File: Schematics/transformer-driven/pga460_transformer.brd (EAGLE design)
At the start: 20 parts, among them IC1 PGA460TPWQ1, T1 B78416A2232A003

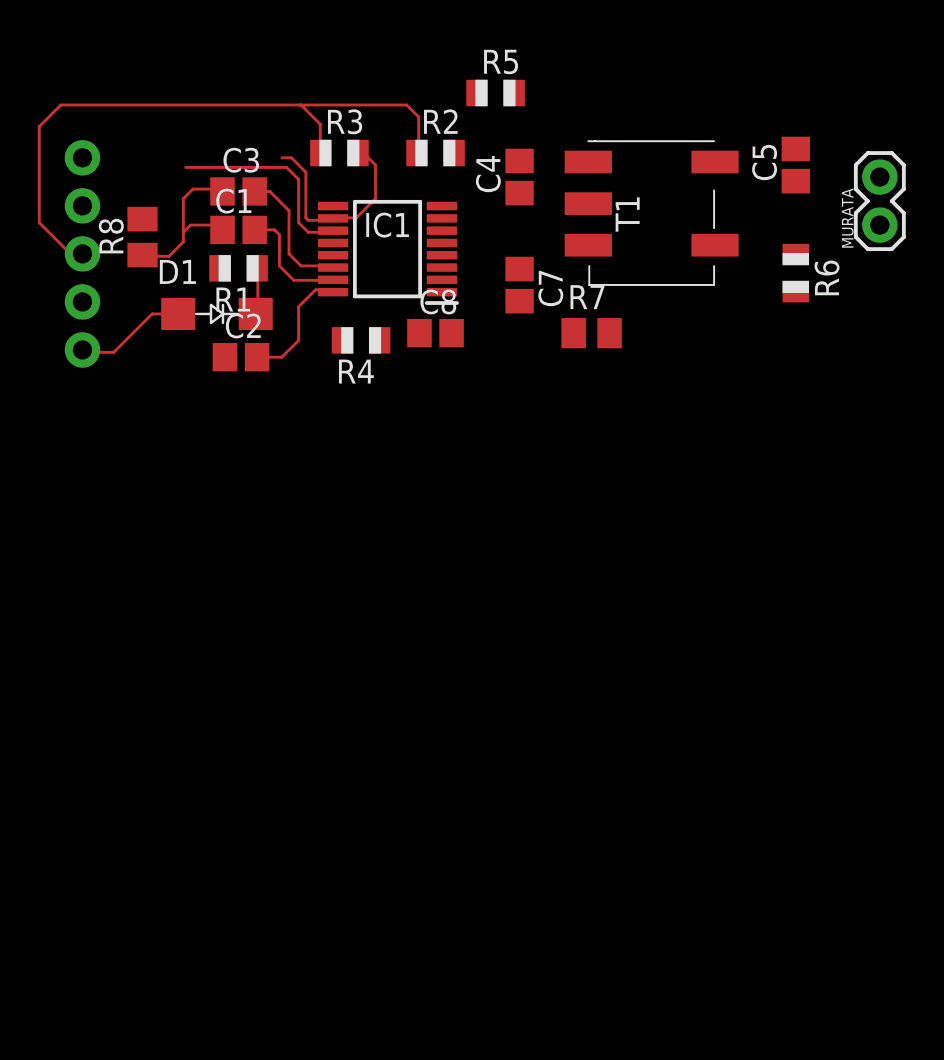
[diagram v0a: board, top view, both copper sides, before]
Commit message: update report. add in mega shield template.
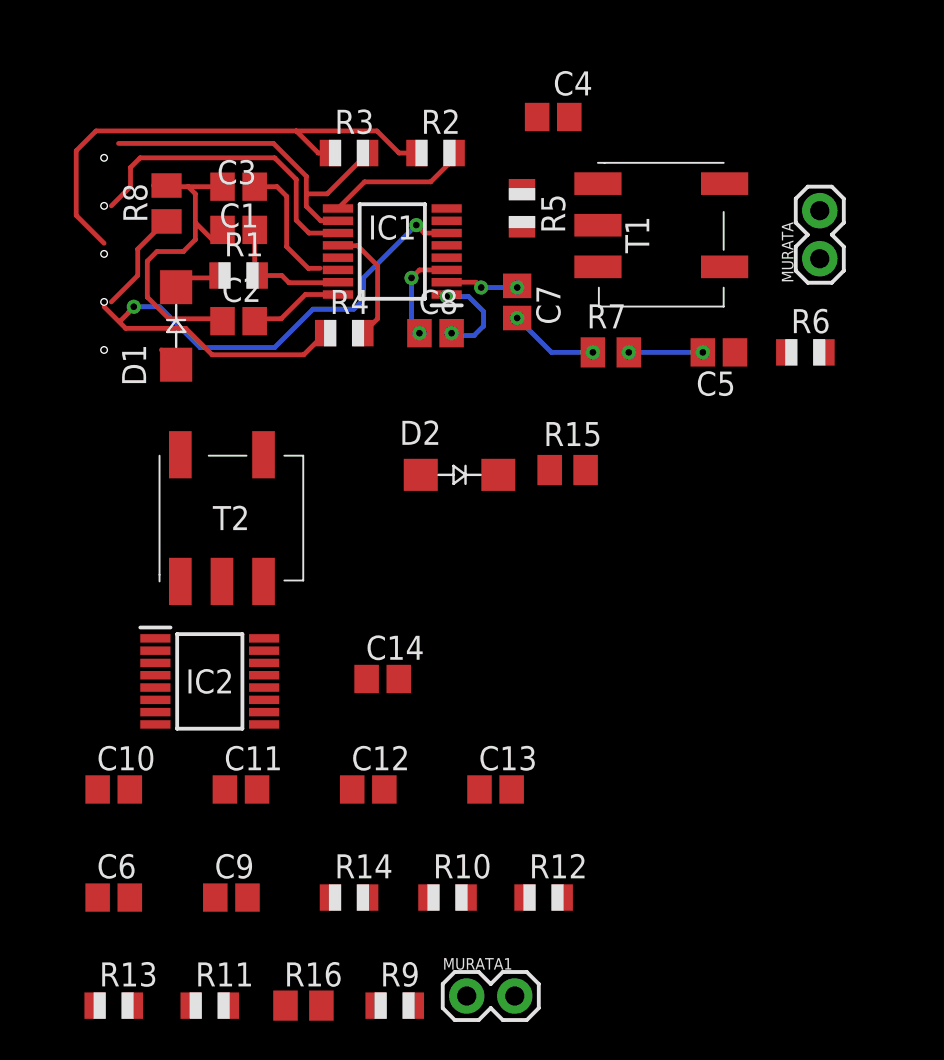
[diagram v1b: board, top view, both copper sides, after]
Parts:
- removed J1: (no value), SparkFun-Connectors:1X05
- added C10: 100uF, adafruit:C0805
- added C11: 680pF, adafruit:C0805
- added C12: 0.1 uF, adafruit:C0805
- added C13: 390pF, adafruit:C0805
- added C14: 0.033uF, adafruit:C0805
- added C6, C9: 0.1uF, adafruit:C0805
- added D2: 1N4007, casovac:SMA
- added IC2: PGA460TPWQ1, PGA460TPWQ1:SOP65P640X120-16N
- added MURATA1: ma59mf14-7n, SparkFun-Connectors:1X02
- added R10, R11, R12: 10k, adafruit:R0805
- added R13: 100, adafruit:R0805
- added R14: 2.7k, adafruit:R0805
- added R15: 3K, rcl:M0805
- added R16: 0, adafruit:M0805
- added R9: 10, adafruit:R0805
- added T2: B78416A2232A003, SamacSys_Parts:B78416A2232A003
- moved C5 10.7 mm to (14.2, -34.7), turned to 180 degrees
- moved R5 6.25 mm to (3.81, -27.1), turned to 270 degrees
- moved R6 4.22 mm to (18.8, -34.7), turned to 0 degrees
- moved MURATA 3.64 mm to (19.6, -29.7)
- moved C4 3.64 mm to (5.46, -22.2), turned to 0 degrees
- moved D1 2.25 mm to (-14.5, -33.3), turned to 90 degrees
- moved R8 2.18 mm to (-15.0, -26.8)
- moved C2 1.91 mm to (-11.2, -33.0)
- moved R7 1.44 mm to (8.51, -34.7)
- moved T1 1.25 mm to (11.2, -28.4)
- moved R4 0.97 mm to (-5.59, -33.7), turned to 0 degrees
- moved C7 0.90 mm to (3.56, -32.0)
- moved R3 0.51 mm to (-5.33, -24.1)
- moved R1 0.38 mm to (-11.2, -30.6), turned to 0 degrees
- moved IC1 0.28 mm to (-3.05, -29.3)
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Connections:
- removed net N$5: IC1.12, R4.2
- new net N$11: D2.K, R9.1
- new net N$12: C11.2, MURATA1.1, R14.1, R15.2, T2.4
- new net N$13: C13.2, R15.1
- new net N$7: C9.2, IC2.14
- new net N$9: C12.2, IC2.16
- new net SCLK: IC1.12, IC2.12, R12.2, R4.2
- new net TEST: IC1.9, IC2.9, R10.2, R2.2
- net 5V: now also R10.1, R11.1; no longer J1.3
- net GND: now also C10.1, C11.1, C12.1, C14.2, C6.1, C9.1, IC2.1, IC2.4, IC2.6, MURATA1.2, R12.1, R14.2, R16.1, R16.2, T2.6; no longer J1.4
- net INN: now also C14.1, IC2.3
- net INP: now also C13.1, IC2.2
- net N$6: now also C6.2, IC2.15, R9.2; no longer IC1.9, R2.2
- net OUTA: now also IC2.5, T2.1
- net OUTB: now also IC2.7, T2.3
- net RXD: now also IC2.11; no longer J1.2
- net TXD: now also IC2.10, R11.2; no longer J1.1
- net VPWR: now also C10.2, D2.A, R13.1, R13.2, T2.2; no longer J1.5
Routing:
- net GND: track 0.00 -> 65.7 mm, vias 0 -> 4
- net N$16: track 33.1 -> 0.00 mm
- net 5V: track 0.00 -> 26.7 mm
- net TXD: track 0.00 -> 18.4 mm
- net RXD: track 0.00 -> 16.5 mm
- net N$14: track 10.5 -> 0.00 mm
- net N$15: track 8.81 -> 0.00 mm
- net TEST: track 0.00 -> 7.53 mm
- net N$1: track 0.00 -> 7.04 mm
- net N$2: track 0.00 -> 6.82 mm
- net N$9: track 6.78 -> 0.00 mm
- net SCLK: track 0.00 -> 6.43 mm
- net N$7: track 6.32 -> 0.00 mm
- net N$11: track 6.01 -> 0.00 mm
- net INN: track 0.00 -> 5.25 mm, vias 0 -> 2
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
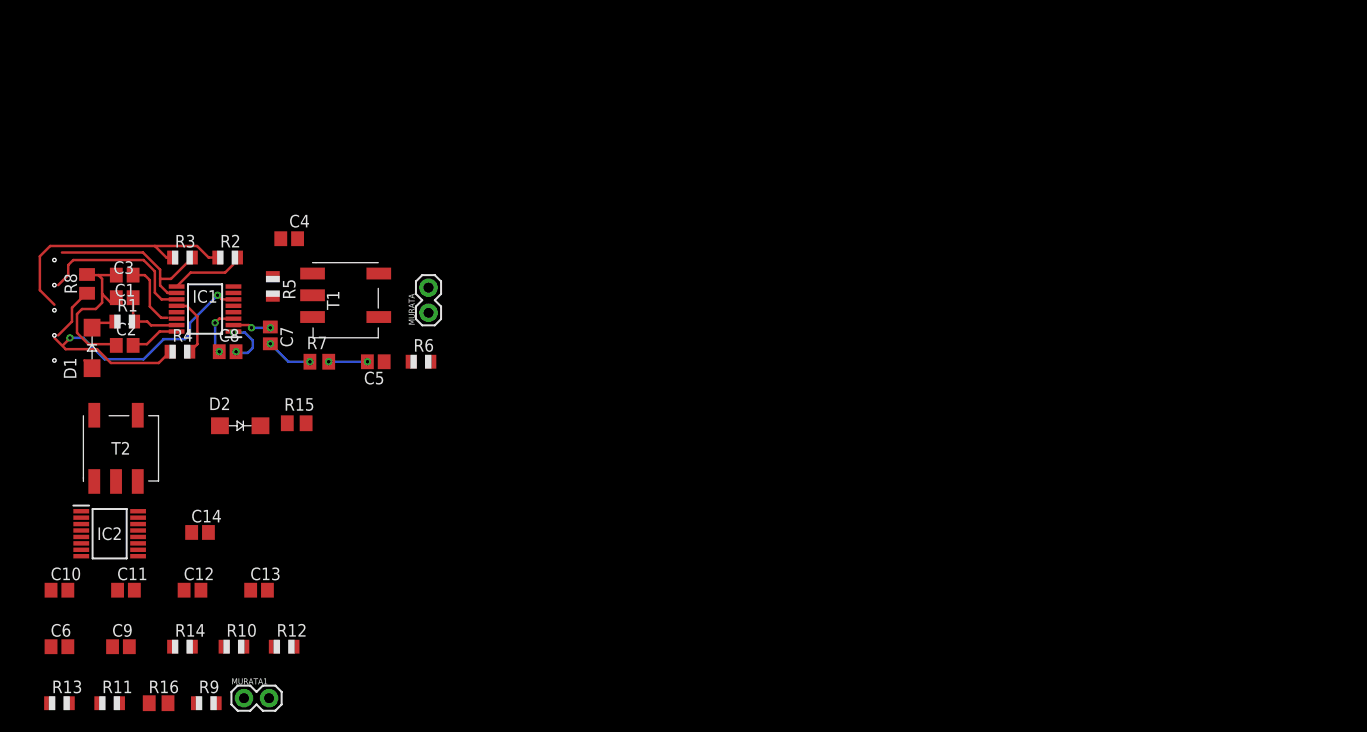
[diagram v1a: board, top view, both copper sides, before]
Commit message: update layout for transformer-driven
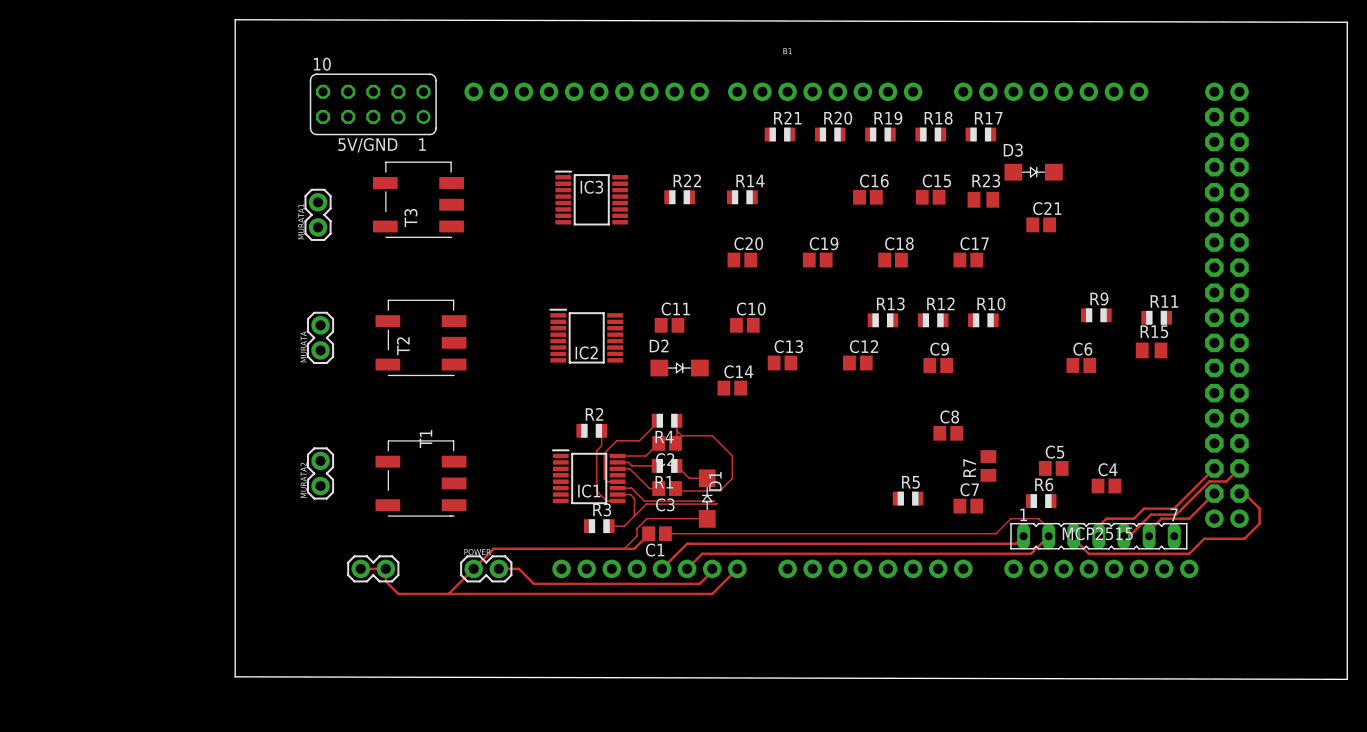
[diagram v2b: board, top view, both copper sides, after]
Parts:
- removed R16, R8: 0, adafruit:M0805
- added 5V/GND: (no value), con-lsta:FE05-2
- added B1: ARDUINO_MEGA_R3FULL, SparkFun-Boards:ARDUINO_MEGA_NO_SILK
- added C15, C16: 0.1uF, adafruit:C0805
- added C17: 100uF, adafruit:C0805
- added C18: 680pF, adafruit:C0805
- added C19: 0.1 uF, adafruit:C0805
- added C20: 390pF, adafruit:C0805
- added C21: 0.033uF, adafruit:C0805
- added D3: 1N4007, casovac:SMA
- added IC3: PGA460TPWQ1, PGA460TPWQ1:SOP65P640X120-16N
- added MCP2515: (no value), con-lsta:FE07
- added MURATA2: ma59mf14-7n, SparkFun-Connectors:1X02
- added POWER, VIN: (no value), SparkFun-Connectors:1X02
- added R17: 10, adafruit:R0805
- added R18, R19, R20: 10k, adafruit:R0805
- added R21: 100, adafruit:R0805
- added R22: 2.7k, adafruit:R0805
- added R23: 3K, rcl:M0805
- added T3: B78416A2232A003, SamacSys_Parts:B78416A2232A003
- moved R11 112.9 mm to (93.2, -30.2)
- moved C6 107.2 mm to (85.6, -35.1)
- moved R9 98.2 mm to (87.1, -30.0)
- moved R13 91.9 mm to (65.5, -30.5)
- moved C9 87.4 mm to (71.1, -35.1)
- moved R15 86.8 mm to (92.7, -33.5)
- moved C4 86.4 mm to (88.1, -47.2)
- moved R10 82.7 mm to (75.7, -30.5)
- moved C10 74.3 mm to (51.6, -31.0)
- moved R12 73.5 mm to (70.6, -30.5)
- moved C8 73.4 mm to (72.1, -41.9)
- moved C7 72.7 mm to (74.2, -49.3), turned to 0 degrees
- moved R14 72.6 mm to (51.3, -18.0)
- moved C12 71.1 mm to (63.0, -34.8)
- moved C5 69.4 mm to (82.8, -45.5), turned to 0 degrees
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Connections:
- net N$2 renamed IOREG1
- net N$3 renamed AVDD1
- net N$7 renamed IOREG2
- net N$9 renamed AVDD2
- removed net INN: C14.1, C8.1, IC1.3, IC2.3
- removed net INP: C13.1, C7.1, IC1.2, IC2.2
- removed net N$1: C1.2, IC1.15, R1.2
- removed net N$6: C6.2, IC2.15, R9.2
- removed net OUTA: IC1.5, IC2.5, T1.1, T2.1
- removed net OUTB: IC1.7, IC2.7, T1.3, T2.3
- removed net RXD: IC1.11, IC2.11
- removed net TXD: IC1.10, IC2.10, R11.2, R3.2
- new net AVDD3: C19.2, IC3.16
- new net CS: B1.53, MCP2515.3
- new net INN_1: C8.1, IC1.3
- new net INN_2: C14.1, IC2.3
- new net INN_3: C21.1, IC3.3
- new net INP_1: C7.1, IC1.2
- new net INP_2: C13.1, IC2.2
- new net INP_3: C20.1, IC3.2
- new net INT: MCP2515.7
- new net IOREG3: C16.2, IC3.14
- new net MISO: B1.50, MCP2515.4
- new net MOSI: B1.51, MCP2515.5
- new net N$16: D3.K, R17.1
- new net N$17: C18.2, MURATA2.1, R22.1, R23.2, T3.4
- new net N$18: C20.2, R23.1
- new net OUTA_1: IC1.5, T1.1
- new net OUTA_2: IC2.5, T2.1
- new net OUTA_3: IC3.5, T3.1
- new net OUTB_1: IC1.7, T1.3
- new net OUTB_2: IC2.7, T2.3
- new net OUTB_3: IC3.7, T3.3
- new net RX1: B1.19, IC1.11
- new net RX2: B1.17, IC2.11
- new net RX3: B1.15, IC3.11
- new net SCLK1: IC1.12, R4.2
- new net SCLK2: IC2.12, R12.2
- new net SCLK3: IC3.12, R20.2
- new net TX1: B1.18, IC1.10, R3.2
- new net TX2: B1.16, IC2.10, R11.2
- new net TX3: B1.14, IC3.10, R19.2
- new net VIN: B1.VIN, C1.2, C15.2, C6.2, D1.A, D2.A, D3.A, IC1.15, IC2.15, IC3.15, POWER.1, R1.2, R13.2, R17.2, R21.2, R5.2, R9.2, VIN.1, VIN.2
- net 5V: now also 5V/GND.1, 5V/GND.3, 5V/GND.5, 5V/GND.7, 5V/GND.9, B1.5V, B1.5V@1, B1.5V@2, MCP2515.1, R18.1, R19.1
- net GND: now also 5V/GND.10, 5V/GND.2, 5V/GND.4, 5V/GND.6, 5V/GND.8, B1.GND, B1.GND@1, B1.GND@3, B1.GND@4, C15.1, C16.1, C17.1, C18.1, C19.1, C21.2, IC3.1, IC3.4, IC3.6, MCP2515.2, MURATA2.2, POWER.2, R20.1, R22.2, T3.6; no longer R16.1, R16.2, R8.1, R8.2
- net SCLK: now also B1.52, MCP2515.6; no longer IC1.12, IC2.12, R12.2, R4.2
- net TEST: now also IC3.9, R18.2
- net VPWR: now also C17.2, R21.1, T3.2; no longer D1.A, D2.A, R13.2, R5.2
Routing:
- net VIN: track 0.00 -> 78.2 mm
- net GND: track 65.7 -> 120.0 mm, vias 4 -> 0
- net CS: track 0.00 -> 25.1 mm
- net TXD: track 18.4 -> 0.00 mm
- net RXD: track 16.5 -> 0.00 mm
- net TX1: track 0.00 -> 15.6 mm
- net MISO: track 0.00 -> 15.1 mm
- net MOSI: track 0.00 -> 14.5 mm
- net 5V: track 26.7 -> 38.5 mm
- net SCLK1: track 0.00 -> 10.9 mm
- net RX1: track 0.00 -> 10.4 mm
- net N$1: track 7.04 -> 0.00 mm
- net INN: track 5.25 -> 0.00 mm, vias 2 -> 0
- net N$10: track 4.76 -> 0.00 mm, vias 2 -> 0
- net N$8: track 3.92 -> 0.00 mm, vias 2 -> 0
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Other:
- board outline added: 112.5 x 66.7 mm

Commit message: update layout
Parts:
- moved 5V/GND 77.2 mm to (90.4, -19.6), turned to 90 degrees
- moved C5 65.6 mm to (17.3, -48.5), turned to 90 degrees
- moved R6 63.4 mm to (18.3, -44.5), turned to 270 degrees
- moved R15 59.0 mm to (34.0, -26.9), turned to 180 degrees
- moved C4 56.3 mm to (32.0, -51.3), turned to 180 degrees
- moved C18 49.7 mm to (17.3, -18.0), turned to 90 degrees
- moved R11 48.4 mm to (45.2, -36.6)
- moved C21 47.8 mm to (34.0, -15.5), turned to 180 degrees
- moved R23 42.4 mm to (34.0, -10.4), turned to 180 degrees
- moved R7 42.1 mm to (34.3, -41.7), turned to 180 degrees
- moved R5 41.8 mm to (26.4, -51.8)
- moved R13 40.7 mm to (25.4, -37.1)
- moved C17 40.4 mm to (34.0, -20.1), turned to 180 degrees
- moved C7 40.2 mm to (34.3, -44.5), turned to 180 degrees
- moved C8 38.2 mm to (34.3, -46.7), turned to 180 degrees
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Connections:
- net N$11 renamed S2+
- net N$17 renamed S3+
- net N$8 renamed S1+
- removed net N$16: D3.K, R17.1
- removed net N$4: D1.K, R1.1
- removed net N$9: D2.K, R9.1
- removed net TEST: IC1.9, IC2.9, IC3.9, R10.2, R18.2, R2.2
- removed net VPWR: C10.2, C17.2, C4.2, R13.1, R21.1, R5.1, T1.2, T2.2, T3.2
- new net S2-: C11.1, C14.2, C5.1, C8.2, MURATA.2, MURATA1.2, R14.2, R6.2, T1.6, T2.6
- new net S3-: C18.1, C21.2, MURATA2.2, R22.2, T3.6
- new net TEST1: IC1.9, R2.2
- new net TEST2: IC2.9, R10.2
- new net TEST3: IC3.9, R18.2
- net GND: no longer C11.1, C14.2, C18.1, C21.2, C5.1, C8.2, MURATA.2, MURATA1.2, MURATA2.2, R14.2, R22.2, R6.2, T1.6, T2.6, T3.6
- net RX1: now also IC1.10, R3.2; no longer IC1.11
- net RX2: now also IC2.10, R11.2; no longer IC2.11
- net RX3: now also IC3.10, R19.2; no longer IC3.11
- net TX1: now also IC1.11; no longer IC1.10, R3.2
- net TX2: now also IC2.11; no longer IC2.10, R11.2
- net TX3: now also IC3.11; no longer IC3.10, R19.2
- net VIN: now also C10.2, C17.2, C4.2, D1.K, D2.K, D3.K, R1.1, R13.1, R17.1, R21.1, R5.1, R9.1, T1.2, T2.2, T3.2
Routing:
- net GND: track 120.0 -> 500.4 mm, vias 0 -> 8
- net VIN: track 78.2 -> 334.9 mm
- net 5V: track 38.5 -> 155.2 mm, vias 0 -> 6
- net S2-: track 0.00 -> 65.5 mm
- net RX1: track 10.4 -> 69.8 mm
- net RX2: track 0.00 -> 54.5 mm
- net TX2: track 0.00 -> 48.7 mm
- net TX1: track 15.6 -> 63.5 mm
- net S3+: track 0.00 -> 42.2 mm
- net RX3: track 0.00 -> 40.2 mm
- net S1+: track 0.00 -> 35.9 mm
- net TX3: track 0.00 -> 33.8 mm
- net S3-: track 0.00 -> 33.1 mm
- net S2+: track 0.00 -> 32.6 mm
- net OUTA_3: track 0.00 -> 19.2 mm
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
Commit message: update layout
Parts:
- moved MCP2515 4.57 mm to (71.4, -49.5)
- moved R13 1.37 mm to (24.1, -37.6)
- moved R6 1.02 mm to (18.3, -43.4)
- moved C5 0.92 mm to (18.0, -48.0)
- moved 5V/GND 0.80 mm to (91.2, -19.8)
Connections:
- removed net S2-: C11.1, C14.2, C5.1, C8.2, MURATA.2, MURATA1.2, R14.2, R6.2, T1.6, T2.6
- removed net S3-: C18.1, C21.2, MURATA2.2, R22.2, T3.6
- net GND: now also C11.1, C14.2, C18.1, C21.2, C5.1, C8.2, MURATA.2, MURATA1.2, MURATA2.2, R14.2, R22.2, R6.2, T1.6, T2.6, T3.6
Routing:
- net GND: track 500.4 -> 614.7 mm, vias 8 -> 16
- net S2-: track 65.5 -> 0.00 mm
- net S3-: track 33.1 -> 0.00 mm
- net MOSI: track 24.9 -> 41.7 mm, vias 0 -> 2
- net S3+: track 42.2 -> 34.0 mm
- net S1+: track 35.9 -> 30.5 mm
- net CS: track 39.4 -> 43.8 mm
- net SCLK: track 21.0 -> 25.1 mm
- net MISO: track 25.7 -> 29.7 mm
- net S2+: track 32.6 -> 29.2 mm
- net VIN: track 334.9 -> 331.4 mm
- net 5V: track 155.2 -> 156.3 mm
- net RX1: track 69.8 -> 70.5 mm
- net INN_1: track 6.96 -> 7.56 mm
